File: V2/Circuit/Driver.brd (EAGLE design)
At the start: 61.6 x 54.6 mm, 32 parts, among them IC1 DRV8300DIPWR, IC2 CD74HC4049PWR, U1 INA240A1PWR, U2 INA240A1PWR, U3 INA240A1PWR

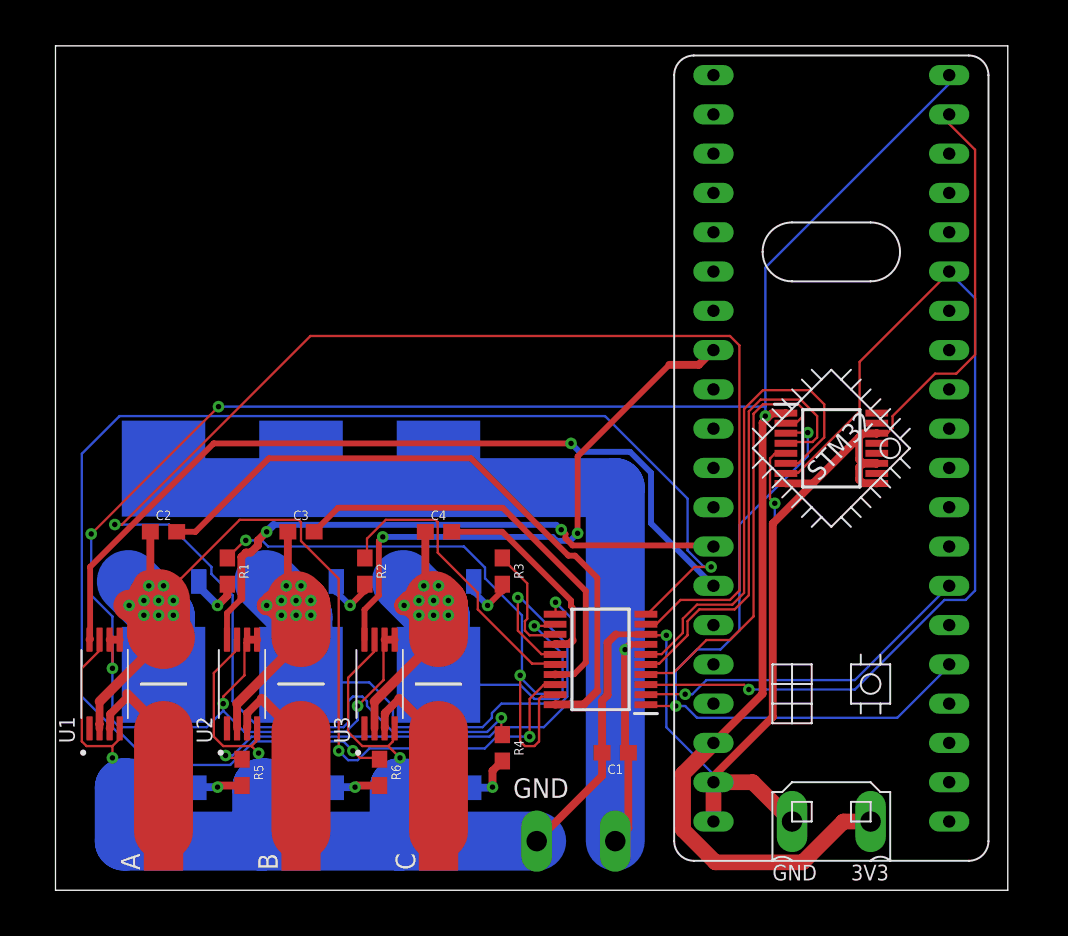
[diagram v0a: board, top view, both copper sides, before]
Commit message: Designed V2, Ready for autoroutering 1
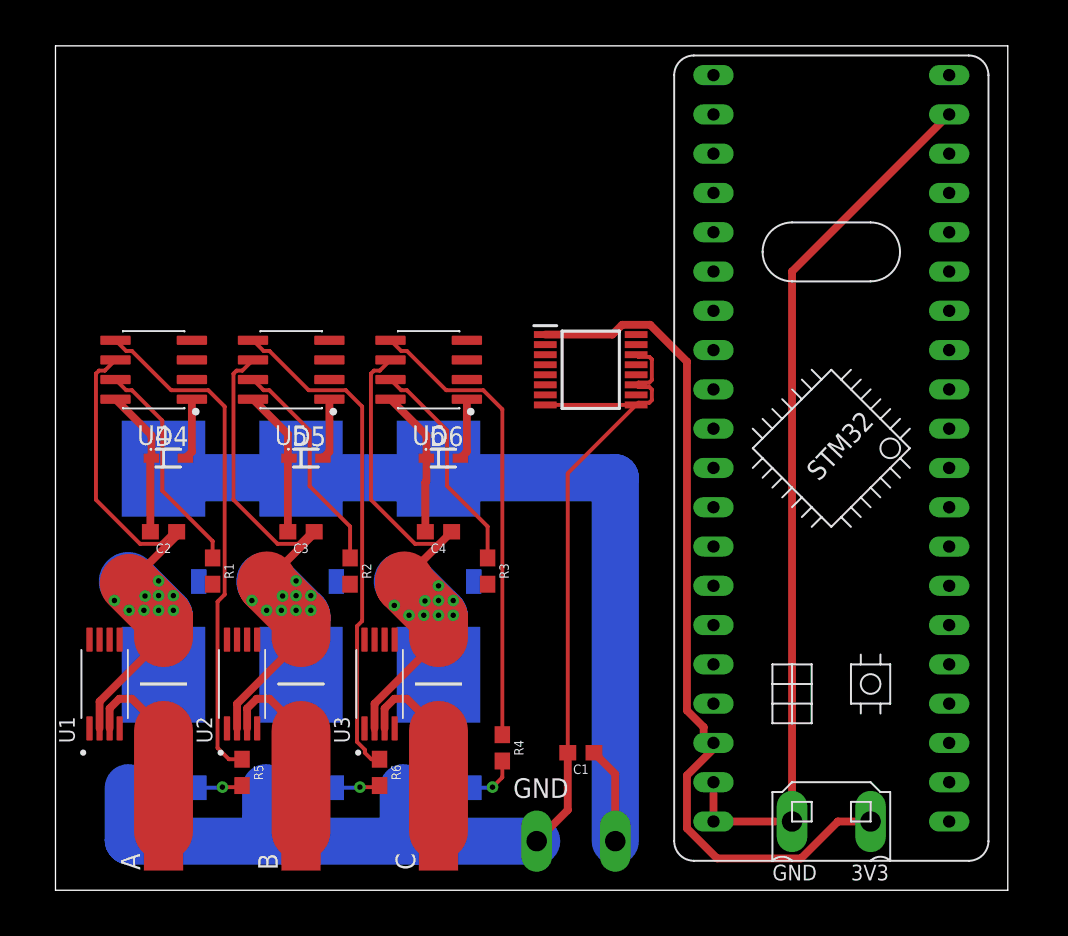
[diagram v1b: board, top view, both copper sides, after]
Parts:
- removed IC1: DRV8300DIPWR, DRV8300DIPWR:SOP65P640X120-20N
- added D4, D5, D6: 1N914BWS, _hhn_diodes_smd:SOD323F
- added U4, U5, U6: SOIC127P610X320-8NSOIC8, SOIC127P610X320-8N:SOIC127P599X175-8N
- moved IC2 16.4 mm to (133.0, 33.0)
- moved C1 2.22 mm to (132.4, 8.26)
- moved R1 0.95 mm to (108.6, 20.0)
- moved R2 0.95 mm to (117.5, 20.0)
- moved R3 0.95 mm to (126.4, 20.0)
- turned C2 to 180 degrees
- turned C3 to 180 degrees
- turned C4 to 180 degrees
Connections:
- net BSTA: now also D4.C, U4.8; no longer IC1.20
- net BSTB: now also D5.C, U5.8; no longer IC1.17
- net BSTC: now also D6.C, U6.8; no longer IC1.14
- net GHA: now also U4.7; no longer IC1.19
- net GHB: now also U5.7; no longer IC1.16
- net GHC: now also U6.7; no longer IC1.13
- net GLA: now also U4.5; no longer IC1.11
- net GLB: now also U5.5; no longer IC1.10
- net GLC: now also U6.5; no longer IC1.9
- net GND: now also U4.4, U5.4, U6.4; no longer IC1.8
- net INHA: now also U4.2; no longer IC1.1
- net INHB: now also U5.2; no longer IC1.2
- net INHC: now also U6.2; no longer IC1.3
- net INLA: now also U4.3; no longer IC1.4
- net INLB: now also U5.3; no longer IC1.5
- net INLC: now also U6.3; no longer IC1.6
- net SHA: now also U4.6; no longer IC1.18
- net SHB: now also U5.6; no longer IC1.15
- net SHC: now also U6.6; no longer IC1.12
- net VCC: now also D4.A, D5.A, D6.A, U4.1, U5.1, U6.1; no longer IC1.7
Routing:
- net 3V3: track 163.5 -> 56.0 mm, vias 6 -> 0
- net GLC: track 107.4 -> 30.1 mm, vias 2 -> 0
- net INHC: track 63.3 -> 0.00 mm, vias 1 -> 0
- net GLB: track 91.1 -> 32.7 mm, vias 2 -> 0
- net PB1: track 54.1 -> 0.00 mm, vias 1 -> 0
- net INHA: track 45.0 -> 0.00 mm, vias 2 -> 0
- net GND: track 177.5 -> 138.6 mm, vias 4 -> 0
- net INHB: track 38.1 -> 0.00 mm, vias 2 -> 0
- net PB0: track 38.0 -> 0.00 mm, vias 2 -> 0
- net PA3: track 36.6 -> 0.00 mm, vias 2 -> 0
- net BSTA: track 42.8 -> 9.56 mm
- net INLC: track 31.8 -> 0.00 mm
- net INLB: track 29.7 -> 0.00 mm
- net INLA: track 27.0 -> 0.00 mm
- net SHA: track 78.4 -> 53.1 mm, vias 11 -> 9
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
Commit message: Designed V2, Ready for autoroutering 2
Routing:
- net GND: track 138.6 -> 164.7 mm
- net VCC: track 74.7 -> 90.5 mm, vias 0 -> 3
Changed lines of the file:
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@@
 <drawing>
 <settings>
-<setting alwaysvectorfont="no"/>
+<setting alwaysvectorfont="yes"/>
 <setting verticaltext="up"/>
 </settings>
@@
 <layer number="27" name="tValues" color="7" fill="1" visible="no" active="yes"/>
 <layer number="28" name="bValues" color="7" fill="1" visible="no" active="yes"/>
-<layer number="29" name="tStop" color="7" fill="3" visible="yes" active="yes"/>
-<layer number="30" name="bStop" color="7" fill="6" visible="yes" active="yes"/>
+<layer number="29" name="tStop" color="7" fill="3" visible="no" active="yes"/>
+<layer number="30" name="bStop" color="7" fill="6" visible="no" active="yes"/>
 <layer number="31" name="tCream" color="7" fill="4" visible="no" active="yes"/>
 <layer number="32" name="bCream" color="7" fill="5" visible="no" active="yes"/>
@@
 <wire x1="136.1161" y1="30.8906" x2="135.9705" y2="30.745" width="0.254" layer="1"/>
 <wire x1="130.0945" y1="30.745" x2="135.9705" y2="30.745" width="0.254" layer="1"/>
-<wire x1="135.9705" y1="30.745" x2="131.5475" y2="26.322" width="0.254" layer="1"/>
-<wire x1="131.5475" y1="26.322" x2="131.5475" y2="8.255" width="0.254" layer="1"/>
 <wire x1="140.97" y1="6.35" x2="140.97" y2="3.81" width="0.508" layer="1"/>
 <wire x1="140.97" y1="3.81" x2="146.05" y2="3.81" width="0.508" layer="1"/>
@@
 <wire x1="131.5475" y1="8.255" x2="131.5475" y2="4.5475" width="0.508" layer="1"/>
 <wire x1="131.5475" y1="4.5475" x2="129.54" y2="2.54" width="0.508" layer="1"/>
-<wire x1="130.0945" y1="30.745" x2="125.0251" y2="34.925" width="0" layer="19" extent="1-1"/>
+<wire x1="110.079125" y1="35.63235" x2="112.310675" y2="35.63235" width="0.508" layer="1"/>
+<wire x1="107.2451" y1="34.925" x2="109.371775" y2="34.925" width="0.508" layer="1"/>
+<wire x1="113.018025" y1="34.925" x2="116.1351" y2="34.925" width="0.508" layer="1"/>
+<wire x1="109.371775" y1="34.925" x2="110.079125" y2="35.63235" width="0.508" layer="1"/>
+<wire x1="112.310675" y1="35.63235" x2="113.018025" y2="34.925" width="0.508" layer="1"/>
+<wire x1="118.969125" y1="35.63235" x2="121.200675" y2="35.63235" width="0.508" layer="1"/>
+<wire x1="116.1351" y1="34.925" x2="118.261775" y2="34.925" width="0.508" layer="1"/>
+<wire x1="121.908025" y1="34.925" x2="125.0251" y2="34.925" width="0.508" layer="1"/>
+<wire x1="118.261775" y1="34.925" x2="118.969125" y2="35.63235" width="0.508" layer="1"/>
+<wire x1="121.200675" y1="35.63235" x2="121.908025" y2="34.925" width="0.508" layer="1"/>
+<wire x1="128.9506" y1="31.0016625" x2="129.1886625" y2="30.7636" width="0.508" layer="1"/>
+<wire x1="129.1886625" y1="30.7636" x2="130.0759" y2="30.7636" width="0.508" layer="1"/>
+<wire x1="130.0759" y1="30.7636" x2="130.0945" y2="30.745" width="0.508" layer="1"/>
+<wire x1="125.0251" y1="34.925" x2="125.578225" y2="34.925" width="0.508" layer="1"/>
+<wire x1="125.578225" y1="34.925" x2="128.9506" y2="31.552625" width="0.508" layer="1"/>
+<wire x1="128.9506" y1="31.552625" x2="128.9506" y2="31.0016625" width="0.508" layer="1"/>
+<wire x1="135.9705" y1="30.745" x2="135.9705" y2="12.678" width="0.508" layer="1"/>
+<wire x1="135.9705" y1="12.678" x2="131.5475" y2="8.255" width="0.508" layer="1"/>
+<wire x1="131.5475" y1="8.255" x2="140.97" y2="6.35" width="0" layer="19" extent="1-1"/>
 <wire x1="120.355" y1="9.83" x2="120.91" y2="5.995" width="0" layer="19" extent="1-16"/>
 <wire x1="111.465" y1="9.83" x2="112.02" y2="5.995" width="0" layer="19" extent="1-16"/>
@@
 <wire x1="110.165" y1="15.57" x2="111.465" y2="9.83" width="0" layer="19" extent="1-1"/>
 <wire x1="101.275" y1="15.57" x2="102.575" y2="9.83" width="0" layer="19" extent="1-1"/>
-<wire x1="116.1351" y1="34.925" x2="125.0251" y2="34.925" width="0" layer="19" extent="1-1"/>
-<wire x1="107.2451" y1="34.925" x2="116.1351" y2="34.925" width="0" layer="19" extent="1-1"/>
-<wire x1="140.97" y1="6.35" x2="131.5475" y2="8.255" width="0" layer="19" extent="1-1"/>
 </signal>
 <signal name="3V3">
@@
 <wire x1="102.99455" y1="31.69535" x2="103.368075" y2="31.69535" width="0.254" layer="1"/>
 <wire x1="108.585" y1="21.93236875" x2="108.585" y2="20.8525" width="0.254" layer="1"/>
-<wire x1="105.3306" y1="25.18676875" x2="108.585" y2="21.93236875" width="0.254" layer="1"/>
-<wire x1="103.368075" y1="31.69535" x2="105.3306" y2="29.732825" width="0.254" layer="1"/>
-<wire x1="105.3306" y1="29.732825" x2="105.3306" y2="25.18676875" width="0.254" layer="1"/>
+<wire x1="105.6481" y1="24.86926875" x2="108.585" y2="21.93236875" width="0.254" layer="1"/>
+<wire x1="103.368075" y1="31.69535" x2="105.6481" y2="29.415325" width="0.254" layer="1"/>
+<wire x1="105.6481" y1="29.415325" x2="105.6481" y2="24.86926875" width="0.254" layer="1"/>
 </signal>
 <signal name="SHA">
@@
 <wire x1="125.0251" y1="31.115" x2="125.0251" y2="27.7226" width="0.508" layer="1"/>
 <wire x1="125.0251" y1="27.7226" x2="124.6075" y2="27.305" width="0.508" layer="1"/>
-<wire x1="123.19" y1="26.63" x2="124.6075" y2="27.305" width="0" layer="19" extent="1-16"/>
-<wire x1="115.7175" y1="27.305" x2="123.19" y2="26.63" width="0" layer="19" extent="1-16"/>
-<wire x1="114.3" y1="26.63" x2="115.7175" y2="27.305" width="0" layer="19" extent="1-16"/>
+<wire x1="107.2451" y1="31.115" x2="105.80475" y2="31.115" width="0.508" layer="1"/>
+<wire x1="105.80475" y1="31.115" x2="105.7275" y2="31.03775" width="0.508" layer="1"/>
+<via x="105.7275" y="31.03775" extent="1-16" drill="0.35"/>
+<wire x1="105.7275" y1="31.03775" x2="105.7275" y2="27.94" width="0.508" layer="16"/>
+<wire x1="105.7275" y1="27.94" x2="105.0925" y2="27.305" width="0.508" layer="16"/>
+<wire x1="116.1351" y1="31.115" x2="114.935" y2="31.115" width="0.508" layer="1"/>
+<wire x1="114.935" y1="31.115" x2="114.6175" y2="30.7975" width="0.508" layer="1"/>
+<via x="114.6175" y="30.7975" extent="1-16" drill="0.35"/>
+<wire x1="114.6175" y1="30.7975" x2="114.6175" y2="28.2575" width="0.508" layer="16"/>
+<wire x1="114.6175" y1="28.2575" x2="114.3" y2="27.94" width="0.508" layer="16"/>
+<wire x1="125.0251" y1="31.115" x2="124.94785" y2="31.03775" width="0.508" layer="1"/>
+<wire x1="124.94785" y1="31.03775" x2="123.5075" y2="31.03775" width="0.508" layer="1"/>
+<via x="123.5075" y="31.03775" extent="1-16" drill="0.35"/>
+<wire x1="123.5075" y1="31.03775" x2="123.5075" y2="26.9875" width="0.508" layer="16"/>
+<wire x1="123.5075" y1="26.9875" x2="123.19" y2="26.63" width="0" layer="19" extent="16-16"/>
+<wire x1="116.1351" y1="31.115" x2="123.5075" y2="31.03775" width="0" layer="19" extent="1-1"/>
+<wire x1="114.3" y1="26.63" x2="114.3" y2="27.94" width="0" layer="19" extent="16-16"/>
 <wire x1="105.41" y1="26.63" x2="105.0925" y2="26.035" width="0" layer="19" extent="16-16"/>
+<wire x1="105.0925" y1="27.305" x2="105.41" y2="26.63" width="0" layer="19" extent="16-16"/>
 <wire x1="115.2525" y1="25.4" x2="114.3" y2="26.63" width="0" layer="19" extent="16-16"/>
-<wire x1="106.8275" y1="27.305" x2="105.41" y2="26.63" width="0" layer="19" extent="1-16"/>
 </signal>
 <signal name="N$1">

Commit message: Generated the Gerber files of the circuit
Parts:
- renumbered U$2 to H-A, U$3 to L-A, U$4 to H-B, U$5 to L-B, U$6 to H-C, U$7 to L-C
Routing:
- net 3V3: track 56.0 -> 175.0 mm, vias 0 -> 4
- net PB0: track 0.00 -> 94.9 mm, vias 0 -> 2
- net PA3: track 0.00 -> 93.9 mm, vias 0 -> 1
- net PB1: track 0.00 -> 80.6 mm
- net INHA: track 0.00 -> 61.4 mm, vias 0 -> 2
- net GND: track 164.7 -> 213.0 mm, vias 0 -> 6
- net INHB: track 0.00 -> 47.6 mm, vias 0 -> 2
- net INHC: track 0.00 -> 36.3 mm, vias 0 -> 3
- net INLA: track 0.00 -> 27.5 mm
- net INLB: track 0.00 -> 14.7 mm, vias 0 -> 2
- net INLC: track 0.00 -> 9.10 mm, vias 0 -> 2
- net VCC: track 90.5 -> 97.3 mm
- net N$2: track 0.00 -> 2.89 mm, vias 0 -> 1
- net N$3: track 0.00 -> 2.87 mm, vias 0 -> 1
- net N$1: track 0.00 -> 2.87 mm, vias 0 -> 1
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- added copper zone on layer 16, net BOTTOM
- added copper zone on layer 1, net N$7
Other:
- outline, holes or cut-outs redrawn
